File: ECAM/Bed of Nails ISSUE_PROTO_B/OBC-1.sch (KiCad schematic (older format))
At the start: 19 parts

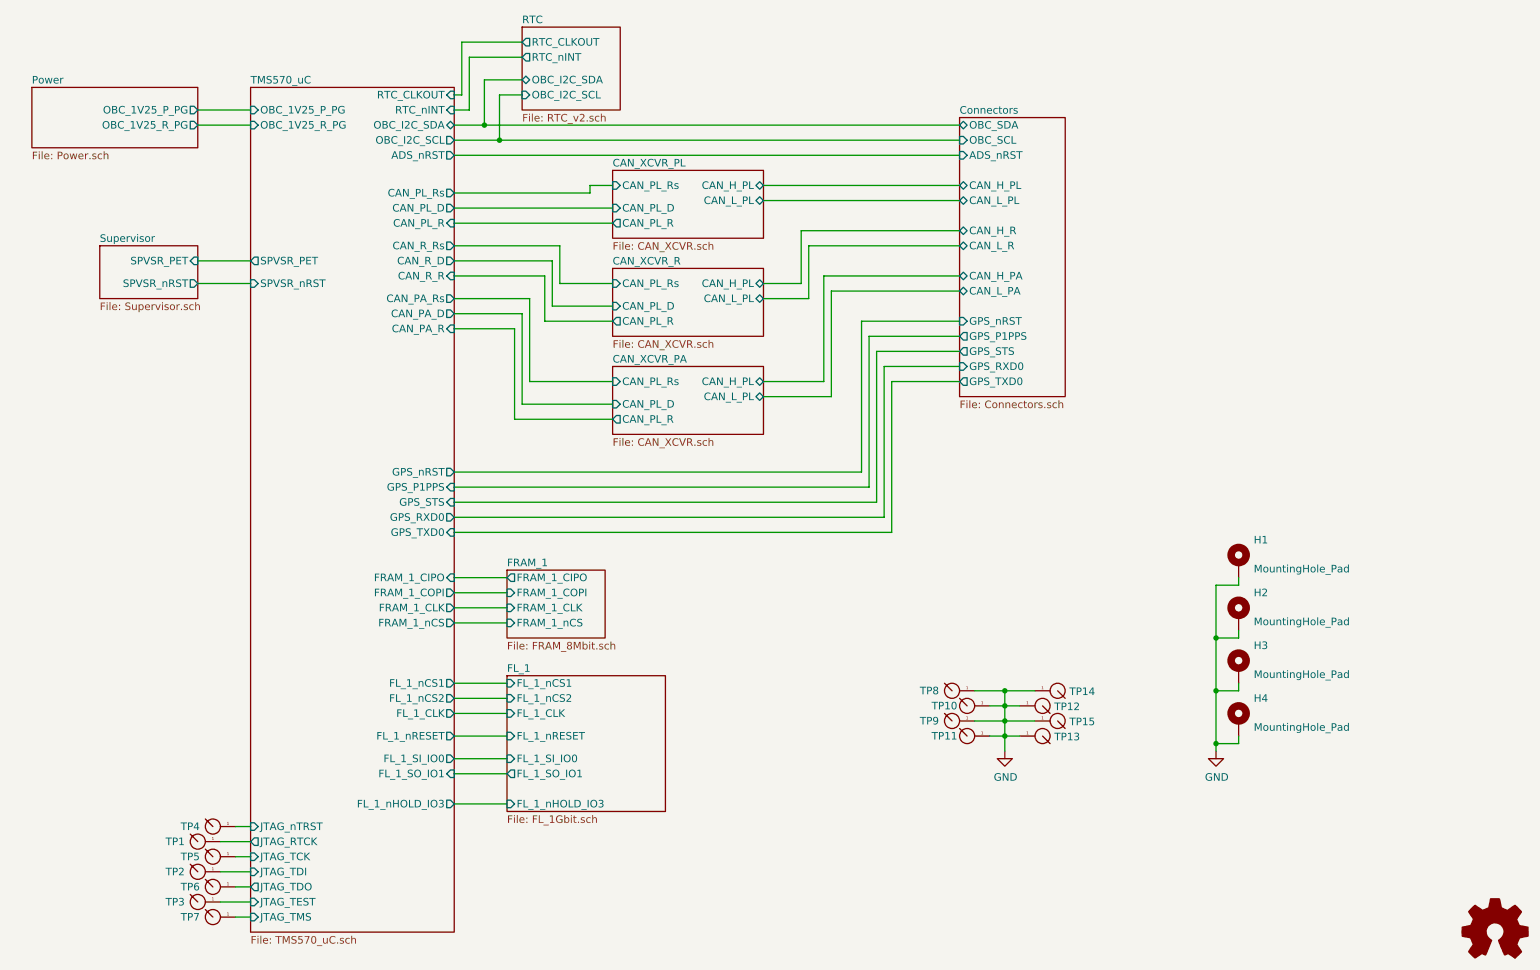
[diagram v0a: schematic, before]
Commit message: set up test points for TSM570 schematic
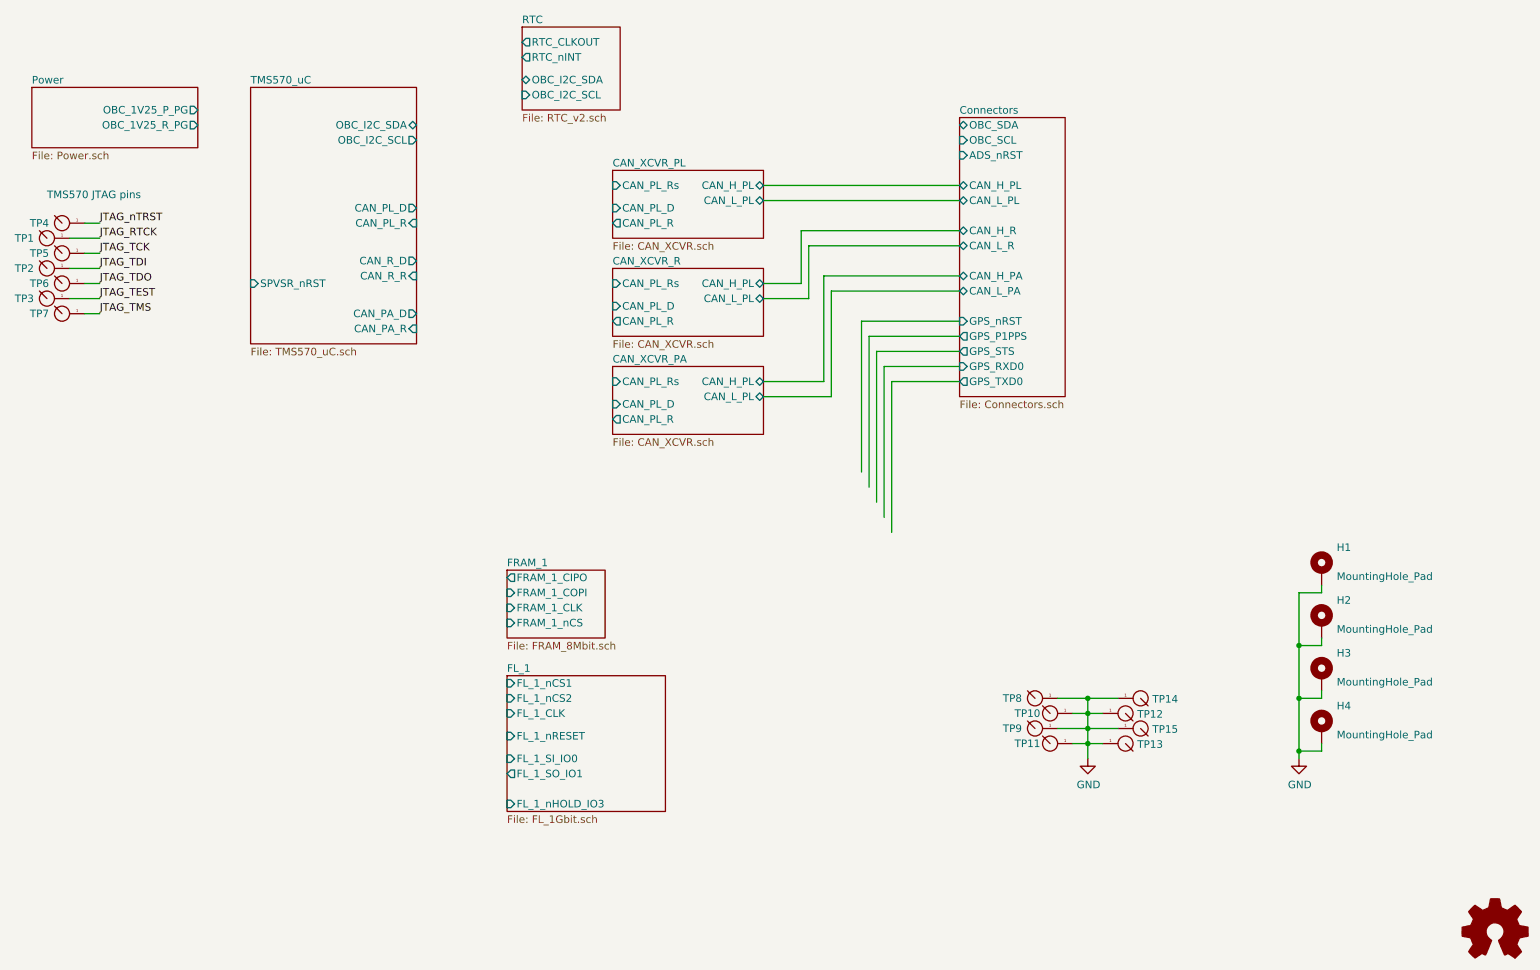
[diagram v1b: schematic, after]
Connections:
- net labels added: JTAG_RTCK, JTAG_TCK, JTAG_TDI, JTAG_TDO, JTAG_TEST, JTAG_TMS, JTAG_nTRST
- wire segments 113 -> 55
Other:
- note added: "TMS570 JTAG pins"
- moved on the sheet: H1, H2, H3, H4, TP1, TP10, TP11, TP12, TP13, TP14, TP15, TP2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

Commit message: cleaned up modules with no current testpoints
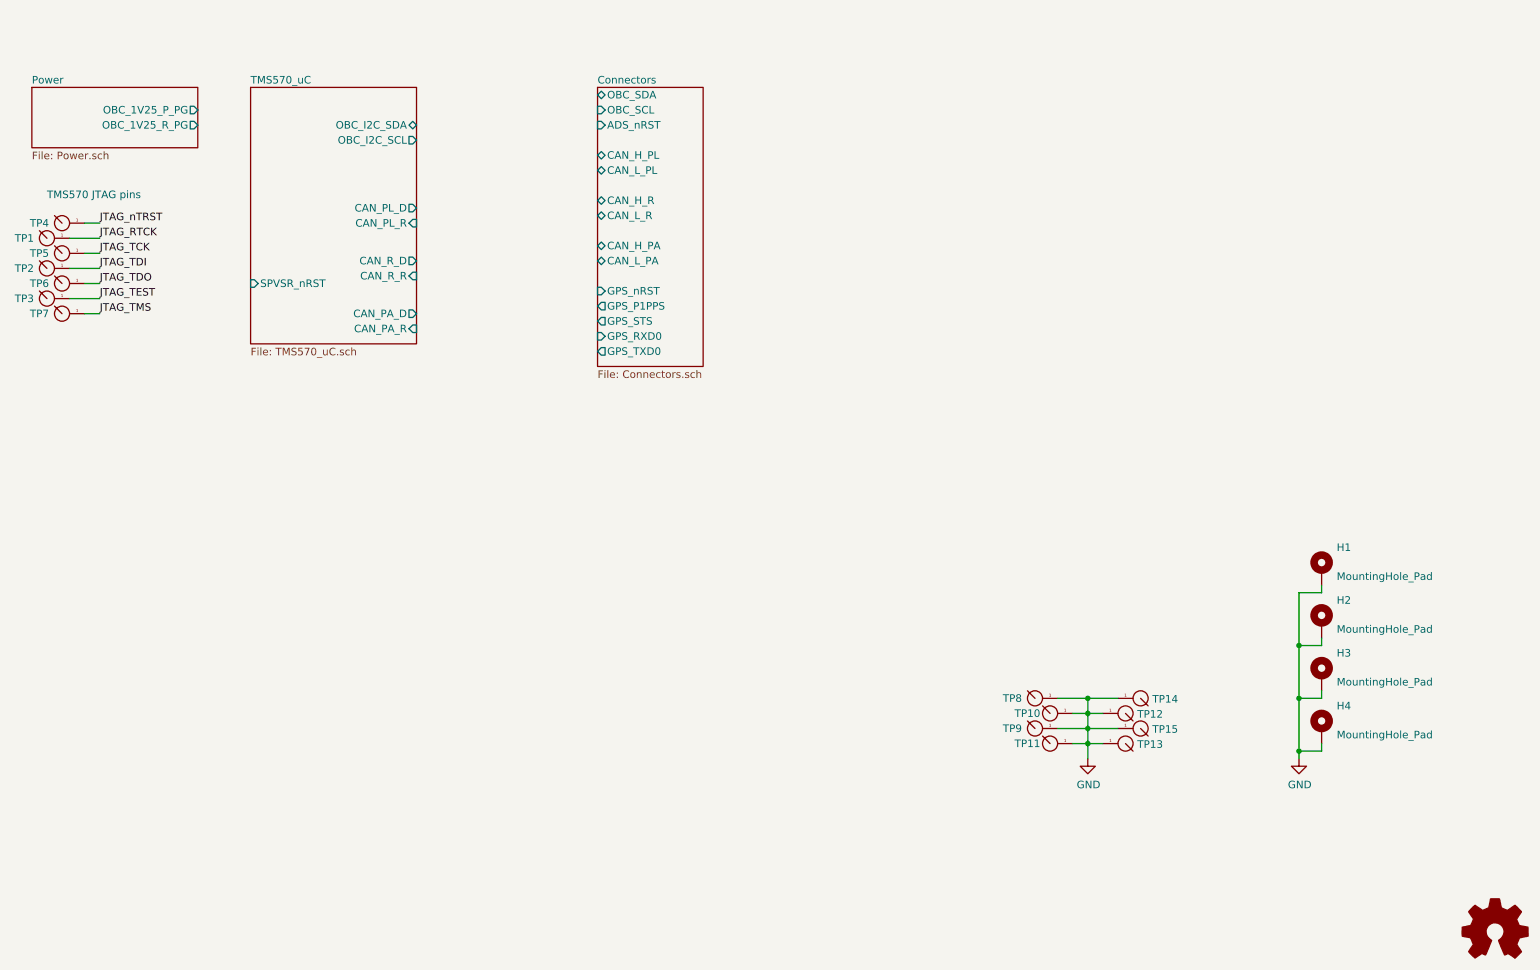
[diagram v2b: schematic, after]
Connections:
- wire segments 55 -> 31
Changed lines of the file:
@@
 $Descr A4 11693 8268
 encoding utf-8
-Sheet 1 10
+Sheet 1 4
 Title "Singularity OBC - Top Level Architecture"
 Date "2021-05-24"
@@
 $EndDescr
 $Sheet
-S 7350 1450 700  1850
+S 4950 1250 700  1850
 U 607BD5B2
 F0 "Connectors" 50
 F1 "Connectors.sch" 50
-F2 "OBC_SDA" B L 7350 1500 50
-F3 "OBC_SCL" I L 7350 1600 50
-F4 "ADS_nRST" I L 7350 1700 50
-F5 "CAN_H_PL" B L 7350 1900 50
-F6 "CAN_L_PL" B L 7350 2000 50
-F7 "CAN_H_R" B L 7350 2200 50
-F8 "CAN_L_R" B L 7350 2300 50
-F9 "CAN_H_PA" B L 7350 2500 50
-F10 "CAN_L_PA" B L 7350 2600 50
-F11 "GPS_STS" O L 7350 3000 50
-F12 "GPS_P1PPS" O L 7350 2900 50
-F13 "GPS_nRST" I L 7350 2800 50
-F14 "GPS_RXD0" I L 7350 3100 50
-F15 "GPS_TXD0" O L 7350 3200 50
+F2 "OBC_SDA" B L 4950 1300 50
+F3 "OBC_SCL" I L 4950 1400 50
+F4 "ADS_nRST" I L 4950 1500 50
+F5 "CAN_H_PL" B L 4950 1700 50
+F6 "CAN_L_PL" B L 4950 1800 50
+F7 "CAN_H_R" B L 4950 2000 50
+F8 "CAN_L_R" B L 4950 2100 50
+F9 "CAN_H_PA" B L 4950 2300 50
+F10 "CAN_L_PA" B L 4950 2400 50
+F11 "GPS_STS" O L 4950 2800 50
+F12 "GPS_P1PPS" O L 4950 2700 50
+F13 "GPS_nRST" I L 4950 2600 50
+F14 "GPS_RXD0" I L 4950 2900 50
+F15 "GPS_TXD0" O L 4950 3000 50
 $EndSheet
-Wire Wire Line
-	6300 2550 6300 2200
-Wire Wire Line
-	6300 2200 7350 2200
-Wire Wire Line
-	6350 2650 6350 2300
-Wire Wire Line
-	6350 2300 7350 2300
-Wire Wire Line
-	6450 3200 6450 2500
-Wire Wire Line
-	6450 2500 7350 2500
-Wire Wire Line
-	6500 3300 6500 2600
-Wire Wire Line
-	6500 2600 7350 2600
-Wire Wire Line
-	6700 3800 6700 2800
-Wire Wire Line
-	6700 2800 7350 2800
-Wire Wire Line
-	6750 3900 6750 2900
-Wire Wire Line
-	6750 2900 7350 2900
-Wire Wire Line
-	6800 4000 6800 3000
-Wire Wire Line
-	6800 3000 7350 3000
-Wire Wire Line
-	6850 4100 6850 3100
-Wire Wire Line
-	6850 3100 7350 3100
-Wire Wire Line
-	6900 4200 6900 3200
-Wire Wire Line
-	6900 3200 7350 3200
 $Comp
 L Graphic:Logo_Open_Hardware_Small #LOGO1
@@
 	1550 2150 1650 2150
 $Sheet
-S 4350 5150 1050 900
-U 6149C473
-F0 "FL_1" 50
-F1 "FL_1Gbit.sch" 50
-F2 "FL_1_nCS1" I L 4350 5200 50
-F3 "FL_1_nCS2" I L 4350 5300 50
-F4 "FL_1_CLK" I L 4350 5400 50
-F5 "FL_1_nRESET" I L 4350 5550 50
-F6 "FL_1_SI_IO0" I L 4350 5700 50
-F7 "FL_1_SO_IO1" O L 4350 5800 50
-F8 "FL_1_nHOLD_IO3" I L 4350 6000 50
-$EndSheet
-$Sheet
-S 4350 4450 650  450
-U 613715E4
-F0 "FRAM_1" 50
-F1 "FRAM_8Mbit.sch" 50
-F2 "FRAM_1_CIPO" O L 4350 4500 50
-F3 "FRAM_1_nCS" I L 4350 4800 50
-F4 "FRAM_1_COPI" I L 4350 4600 50
-F5 "FRAM_1_CLK" I L 4350 4700 50
-$EndSheet
-Wire Wire Line
-	6050 1900 7350 1900
-Wire Wire Line
-	6050 2000 7350 2000
-Wire Wire Line
-	6050 3300 6500 3300
-Wire Wire Line
-	6050 3200 6450 3200
-Wire Wire Line
-	6050 2650 6350 2650
-Wire Wire Line
-	6050 2550 6300 2550
-$Sheet
-S 5050 3100 1000 450
-U 608A2D6B
-F0 "CAN_XCVR_PA" 50
-F1 "CAN_XCVR.sch" 50
-F2 "CAN_H_PL" B R 6050 3200 50
-F3 "CAN_L_PL" B R 6050 3300 50
-F4 "CAN_PL_Rs" I L 5050 3200 50
-F5 "CAN_PL_D" I L 5050 3350 50
-F6 "CAN_PL_R" O L 5050 3450 50
-$EndSheet
-$Sheet
-S 5050 2450 1000 450
-U 608A1F6B
-F0 "CAN_XCVR_R" 50
-F1 "CAN_XCVR.sch" 50
-F2 "CAN_H_PL" B R 6050 2550 50
-F3 "CAN_L_PL" B R 6050 2650 50
-F4 "CAN_PL_Rs" I L 5050 2550 50
-F5 "CAN_PL_D" I L 5050 2700 50
-F6 "CAN_PL_R" O L 5050 2800 50
-$EndSheet
-$Sheet
-S 5050 1800 1000 450
-U 60882301
-F0 "CAN_XCVR_PL" 50
-F1 "CAN_XCVR.sch" 50
-F2 "CAN_H_PL" B R 6050 1900 50
-F3 "CAN_L_PL" B R 6050 2000 50
-F4 "CAN_PL_Rs" I L 5050 1900 50
-F5 "CAN_PL_D" I L 5050 2050 50
-F6 "CAN_PL_R" O L 5050 2150 50
-$EndSheet
-$Sheet
 S 1200 1250 1100 400
 U 607BD428
@@
 F3 "OBC_1V25_R_PG" O R 2300 1500 50
 $EndSheet
-$Sheet
-S 4450 850  650  550
-U 60BB4065
-F0 "RTC" 50
-F1 "RTC_v2.sch" 50
-F2 "OBC_I2C_SDA" B L 4450 1200 50
-F3 "OBC_I2C_SCL" I L 4450 1300 50
-F4 "RTC_CLKOUT" O L 4450 950 50
-F5 "RTC_nINT" O L 4450 1050 50
-$EndSheet
 $Comp

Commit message: file cleanup, .attributes update
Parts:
- added TP? (x7): TEST-POINT, TFT_TestPoints:TP_RDPad_D1.0mm, symbol TFT_testpoints:TEST-POINT
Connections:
- net Connectors/ADS_nRST: now also TP?.1
- net Connectors/CAN_H_PA: now also TP?.1
- net Connectors/CAN_H_PL: now also TP?.1
- net Connectors/CAN_H_R: now also TP?.1
- net Connectors/CAN_L_PA: now also TP?.1
- net Connectors/CAN_L_PL: now also TP?.1
- net Connectors/CAN_L_R: now also TP?.1
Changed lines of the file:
@@
 F19 "OBC_I2C_SDA" B R 3750 1500 50
 F20 "OBC_I2C_SCL" O R 3750 1600 50
-F32 "SPVSR_nRST" I L 2650 2550 50
+F32 "SPVSR_nRST" I R 3750 1850 50
 $EndSheet
 Wire Wire Line
@@
 	1550 2150 1650 2150
 $Sheet
-S 1200 1250 1100 400
+S 2650 3200 1100 400
 U 607BD428
 F0 "Power" 50
 F1 "Power.sch" 50
-F2 "OBC_1V25_P_PG" O R 2300 1400 50
-F3 "OBC_1V25_R_PG" O R 2300 1500 50
+F2 "OBC_1V25_P_PG" O R 3750 3350 50
+F3 "OBC_1V25_R_PG" O R 3750 3450 50
 $EndSheet
 $Comp
@@
 Text Notes 1300 2000 0    50   ~ 0
 TMS570 JTAG pins
+Wire Wire Line
+	3750 1500 3900 1500
+Wire Wire Line
+	3900 1500 3900 1300
+Wire Wire Line
+	3900 1300 4950 1300
+Wire Wire Line
+	3750 1600 4000 1600
+Wire Wire Line
+	4000 1600 4000 1400
+Wire Wire Line
+	4000 1400 4950 1400
+$Comp
+L TFT_testpoints:TEST-POINT TP?
+U 1 1 60CC4740
+P 4600 1500
+F 0 "TP?" H 4400 1500 50  0000 C CNN
+F 1 "TEST-POINT" H 4600 1850 50  0001 C CNN
+F 2 "TFT_TestPoints:TP_RDPad_D1.0mm" H 4600 1500 50  0001 C CNN
+F 3 "" H 4600 1500 50  0001 C CNN
+	1    4600 1500
+	1    0    0    -1
+$EndComp
+Wire Wire Line
+	4700 1500 4950 1500
+Text Label 3950 1850 0    50   ~ 0
+SPVSR_nRST
+Wire Wire Line
+	3950 1850 3750 1850
+Text Label 3950 2050 0    50   ~ 0
+CAN_PL_D
+Text Label 3950 2150 0    50   ~ 0
+CAN_PL_R
+Text Label 3950 2400 0    50   ~ 0
+CAN_R_D
+Text Label 3950 2500 0    50   ~ 0
+CAN_R_R
+Text Label 3950 2750 0    50   ~ 0
+CAN_PA_D
+Text Label 3950 2850 0    50   ~ 0
+CAN_PA_R
+Wire Wire Line
+	3950 2050 3750 2050
+Wire Wire Line
+	3750 2150 3950 2150
+Wire Wire Line
+	3950 2400 3750 2400
+Wire Wire Line
+	3750 2500 3950 2500
+Wire Wire Line
+	3950 2750 3750 2750
+Wire Wire Line
+	3750 2850 3950 2850
+$Comp
+L TFT_testpoints:TEST-POINT TP?
+U 1 1 60CCBFF5
+P 4750 1700
+F 0 "TP?" H 4550 1700 50  0000 C CNN
+F 1 "TEST-POINT" H 4750 2050 50  0001 C CNN
+F 2 "TFT_TestPoints:TP_RDPad_D1.0mm" H 4750 1700 50  0001 C CNN
+F 3 "" H 4750 1700 50  0001 C CNN
+	1    4750 1700
+	1    0    0    -1
+$EndComp
+$Comp
+L TFT_testpoints:TEST-POINT TP?
+U 1 1 60CCC4BB
+P 4750 1800
+F 0 "TP?" H 4550 1800 50  0000 C CNN
+F 1 "TEST-POINT" H 4750 2150 50  0001 C CNN
+F 2 "TFT_TestPoints:TP_RDPad_D1.0mm" H 4750 1800 50  0001 C CNN
+F 3 "" H 4750 1800 50  0001 C CNN
+	1    4750 1800
+	1    0    0    -1
+$EndComp
+$Comp
+L TFT_testpoints:TEST-POINT TP?
+U 1 1 60CCF1A5
+P 4750 2000
+F 0 "TP?" H 4550 2000 50  0000 C CNN
+F 1 "TEST-POINT" H 4750 2350 50  0001 C CNN
+F 2 "TFT_TestPoints:TP_RDPad_D1.0mm" H 4750 2000 50  0001 C CNN
+F 3 "" H 4750 2000 50  0001 C CNN
+	1    4750 2000
+	1    0    0    -1
+$EndComp
+$Comp
+L TFT_testpoints:TEST-POINT TP?
+U 1 1 60CCF1AB
+P 4750 2100
+F 0 "TP?" H 4550 2100 50  0000 C CNN
+F 1 "TEST-POINT" H 4750 2450 50  0001 C CNN
+F 2 "TFT_TestPoints:TP_RDPad_D1.0mm" H 4750 2100 50  0001 C CNN
+F 3 "" H 4750 2100 50  0001 C CNN
+	1    4750 2100
+	1    0    0    -1
+$EndComp
+$Comp
+L TFT_testpoints:TEST-POINT TP?
+U 1 1 60CD0063
+P 4750 2300
+F 0 "TP?" H 4550 2300 50  0000 C CNN
+F 1 "TEST-POINT" H 4750 2650 50  0001 C CNN
+F 2 "TFT_TestPoints:TP_RDPad_D1.0mm" H 4750 2300 50  0001 C CNN
+F 3 "" H 4750 2300 50  0001 C CNN
+	1    4750 2300
+	1    0    0    -1
+$EndComp
+$Comp
+L TFT_testpoints:TEST-POINT TP?
+U 1 1 60CD0069
+P 4750 2400
+F 0 "TP?" H 4550 2400 50  0000 C CNN
+F 1 "TEST-POINT" H 4750 2750 50  0001 C CNN
+F 2 "TFT_TestPoints:TP_RDPad_D1.0mm" H 4750 2400 50  0001 C CNN
+F 3 "" H 4750 2400 50  0001 C CNN
+	1    4750 2400
+	1    0    0    -1
+$EndComp
+Wire Wire Line
+	4850 1700 4950 1700
+Wire Wire Line
+	4950 1800 4850 1800
+Wire Wire Line
+	4850 2000 4950 2000
+Wire Wire Line
+	4850 2100 4950 2100
+Wire Wire Line
+	4850 2300 4950 2300
+Wire Wire Line
+	4850 2400 4950 2400
 $EndSCHEMATC
